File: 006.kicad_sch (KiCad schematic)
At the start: 49 parts, among them J2 Header 1x2 1.25mm, U1 AM6232ASCGHAALWR

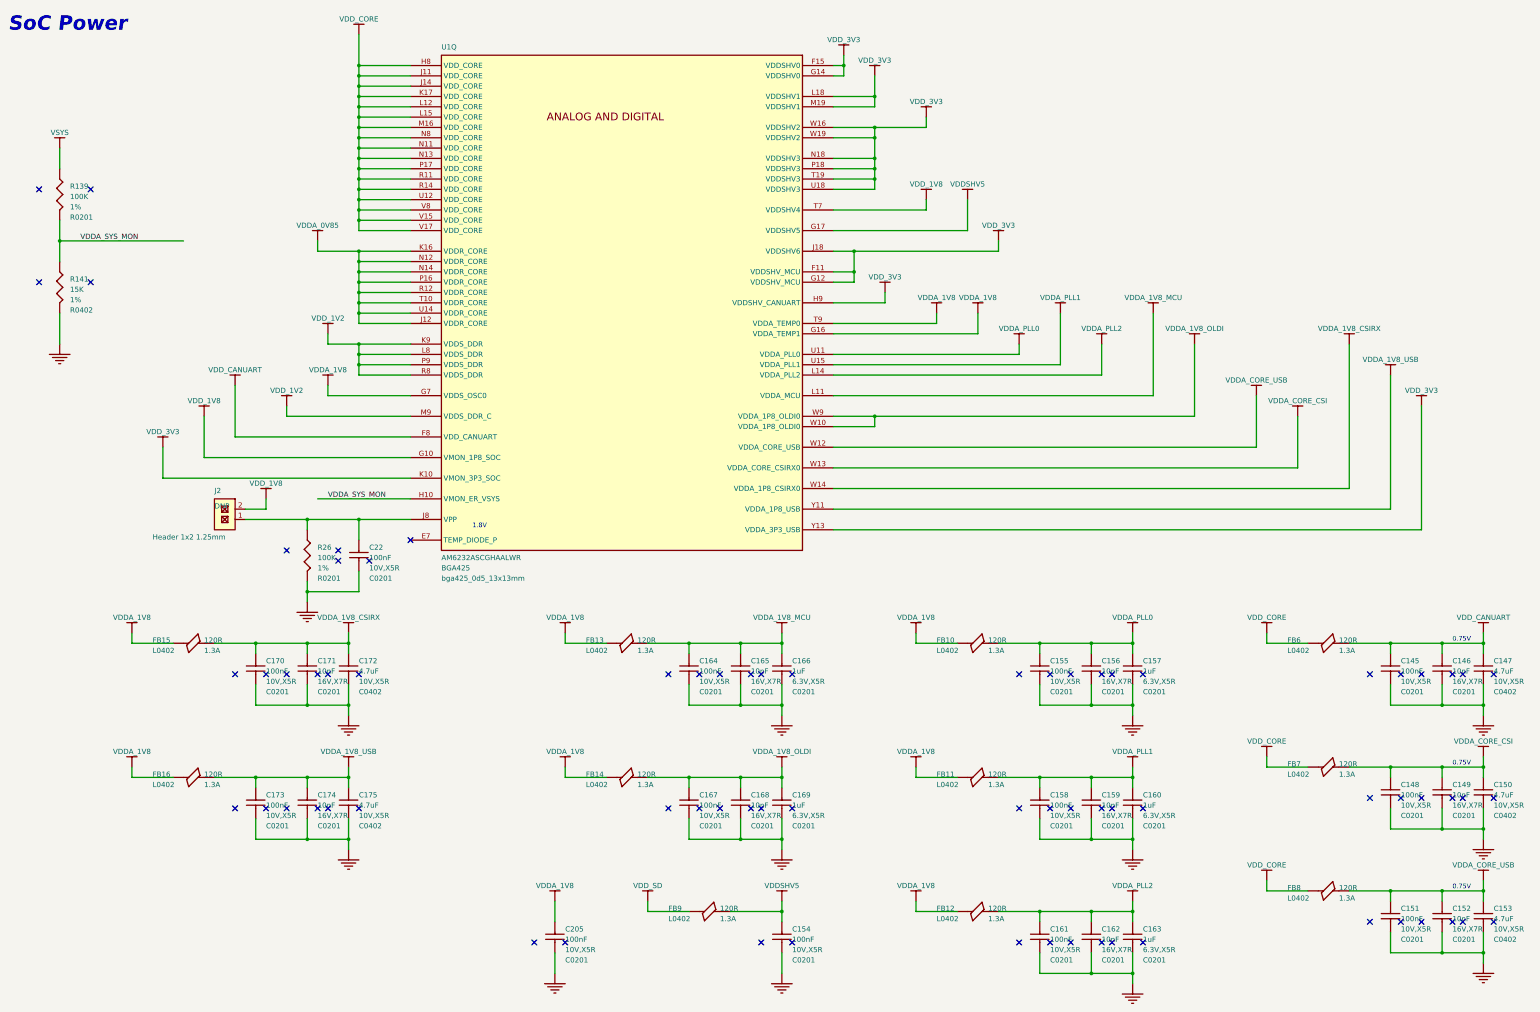
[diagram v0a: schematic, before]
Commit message: Remove rando NCs added during conversion
Also a little tidying.

TODO: check junctions that may be missing. Noticed a few obvious ones
and corrected them already.

Signed-off-by: Michael Welling <mwelling79@gmail.com>
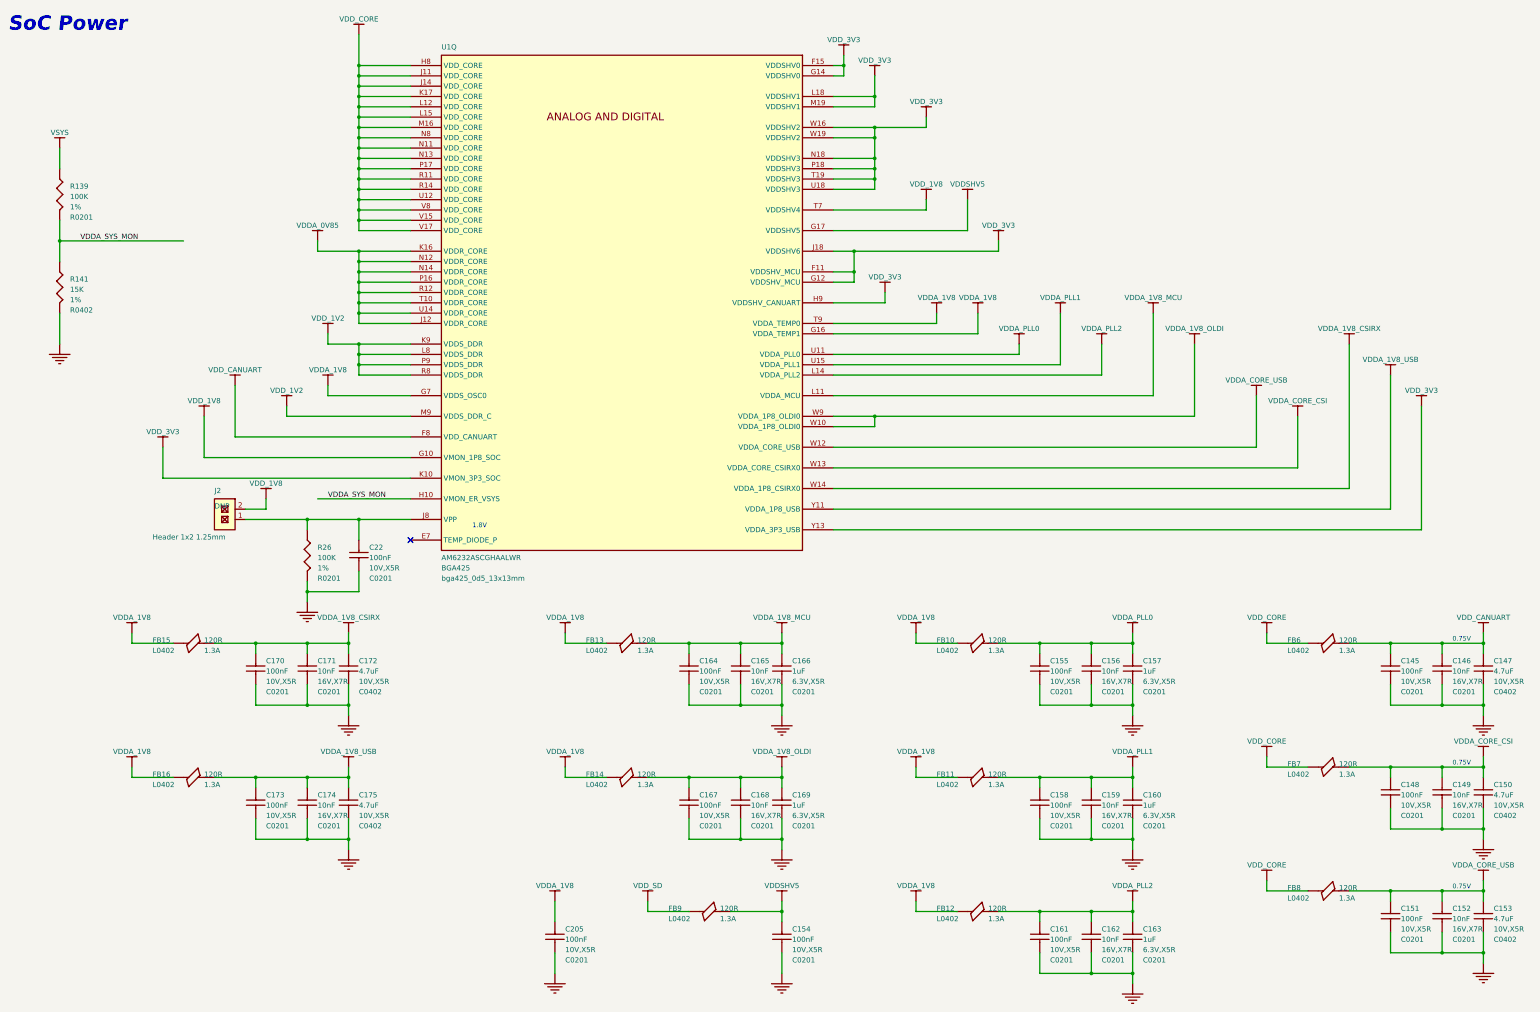
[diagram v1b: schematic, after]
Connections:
- no-connect marks 73 -> 1
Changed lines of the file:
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@@
-	)
-	(no_connect
-		(at 353.06 177.8)
-	)
-	(no_connect
-		(at 266.7 210.82)
-	)
-	(no_connect
-		(at 297.18 210.82)
-	)
-	(no_connect
-		(at 25.4 81.28)
-	)
-	(no_connect
-		(at 38.1 58.42)
-	)
-	(no_connect
-		(at 81.28 177.8)
-	)
-	(no_connect
-		(at 383.54 208.28)
-	)
-	(no_connect
-		(at 193.04 177.8)
-	)
-	(no_connect
-		(at 104.14 177.8)
-	)
-	(no_connect
-		(at 99.06 147.32)
-	)
-	(no_connect
-		(at 73.66 210.82)
-	)
-	(no_connect
-		(at 297.18 243.84)
-	)
-	(no_connect
-		(at 147.32 243.84)
-	)
-	(no_connect
-		(at 266.7 177.8)
-	)
-	(no_connect
-		(at 274.32 177.8)
-	)
-	(no_connect
-		(at 266.7 243.84)
-	)
-	(no_connect
-		(at 383.54 238.76)
-	)
-	(no_connect
-		(at 365.76 177.8)
-	)
-	(no_connect
-		(at 96.52 177.8)
-	)
-	(no_connect
-		(at 154.94 243.84)
-	)
-	(no_connect
-		(at 287.02 177.8)
-	)
-	(no_connect
-		(at 373.38 208.28)
-	)
-	(no_connect
-		(at 25.4 58.42)
-	)
-	(no_connect
-		(at 365.76 208.28)
-	)
-	(no_connect
-		(at 287.02 210.82)
-	)
-	(no_connect
-		(at 38.1 81.28)
-	)
-	(no_connect
-		(at 193.04 210.82)
-	)
-	(no_connect
-		(at 104.14 210.82)
-	)
-	(no_connect
-		(at 375.92 238.76)
-	)
-	(no_connect
-		(at 383.54 177.8)
-	)
-	(no_connect
-		(at 373.38 177.8)
-	)
-	(no_connect
-		(at 274.32 210.82)
-	)
-	(no_connect
-		(at 360.68 208.28)
-	)
-	(no_connect
-		(at 353.06 208.28)
-	)
-	(no_connect
-		(at 187.96 210.82)
-	)
-	(no_connect
-		(at 360.68 177.8)
-	)
-	(no_connect
-		(at 203.2 243.84)
-	)
-	(no_connect
-		(at 180.34 177.8)
-	)
-	(no_connect
-		(at 210.82 243.84)
-	)
-	(no_connect
-		(at 279.4 243.84)
-	)
-	(no_connect
-		(at 203.2 210.82)
-	)
-	(no_connect
-		(at 180.34 210.82)
-	)
-	(no_connect
-		(at 274.32 243.84)
-	)
-	(no_connect
-		(at 106.68 149.86)
-	)
-	(no_connect
-		(at 375.92 177.8)
-	)
-	(no_connect
-		(at 360.68 238.76)
-	)
-	(no_connect
-		(at 287.02 243.84)
-	)
-	(no_connect
-		(at 81.28 210.82)
-	)
-	(no_connect
-		(at 375.92 208.28)
 	)
 	(no_connect
 		(at 116.84 144.78)
 	)
-	(no_connect
-		(at 73.66 177.8)
-	)
-	(no_connect
-		(at 93.98 210.82)
-	)
-	(no_connect
-		(at 200.66 177.8)
-	)
-	(no_connect
-		(at 297.18 177.8)
-	)
-	(no_connect
-		(at 93.98 177.8)
-	)
-	(no_connect
-		(at 289.56 210.82)
-	)
-	(no_connect
-		(at 96.52 210.82)
-	)
-	(no_connect
-		(at 289.56 243.84)
-	)
-	(no_connect
-		(at 365.76 238.76)
-	)
-	(no_connect
-		(at 99.06 149.86)
-	)
-	(no_connect
-		(at 200.66 210.82)
-	)
-	(no_connect
-		(at 86.36 210.82)
-	)
-	(no_connect
-		(at 289.56 177.8)
-	)
-	(no_connect
-		(at 86.36 147.32)
-	)
-	(no_connect
-		(at 353.06 238.76)
-	)
-	(no_connect
-		(at 279.4 177.8)
-	)
-	(no_connect
-		(at 187.96 177.8)
-	)
-	(no_connect
-		(at 373.38 238.76)
-	)
-	(no_connect
-		(at 86.36 177.8)
-	)
-	(no_connect
-		(at 210.82 210.82)
-	)
-	(no_connect
-		(at 279.4 210.82)
-	)
-	(no_connect
-		(at 210.82 177.8)
-	)
-	(no_connect
-		(at 203.2 177.8)
-	)
 	(wire
